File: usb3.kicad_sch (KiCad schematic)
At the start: 50 parts, among them J5 Conn_USB-C_WE_632723300011, Q19 PJE138K, Q4 PJE138K, U17 HD3SS3220RNH, U18 AP22615A_TSOT26, U19 TPD4E05U06QDQARQ1, U20 TPD4E05U06QDQARQ1, U21 TPD4E05U06QDQARQ1

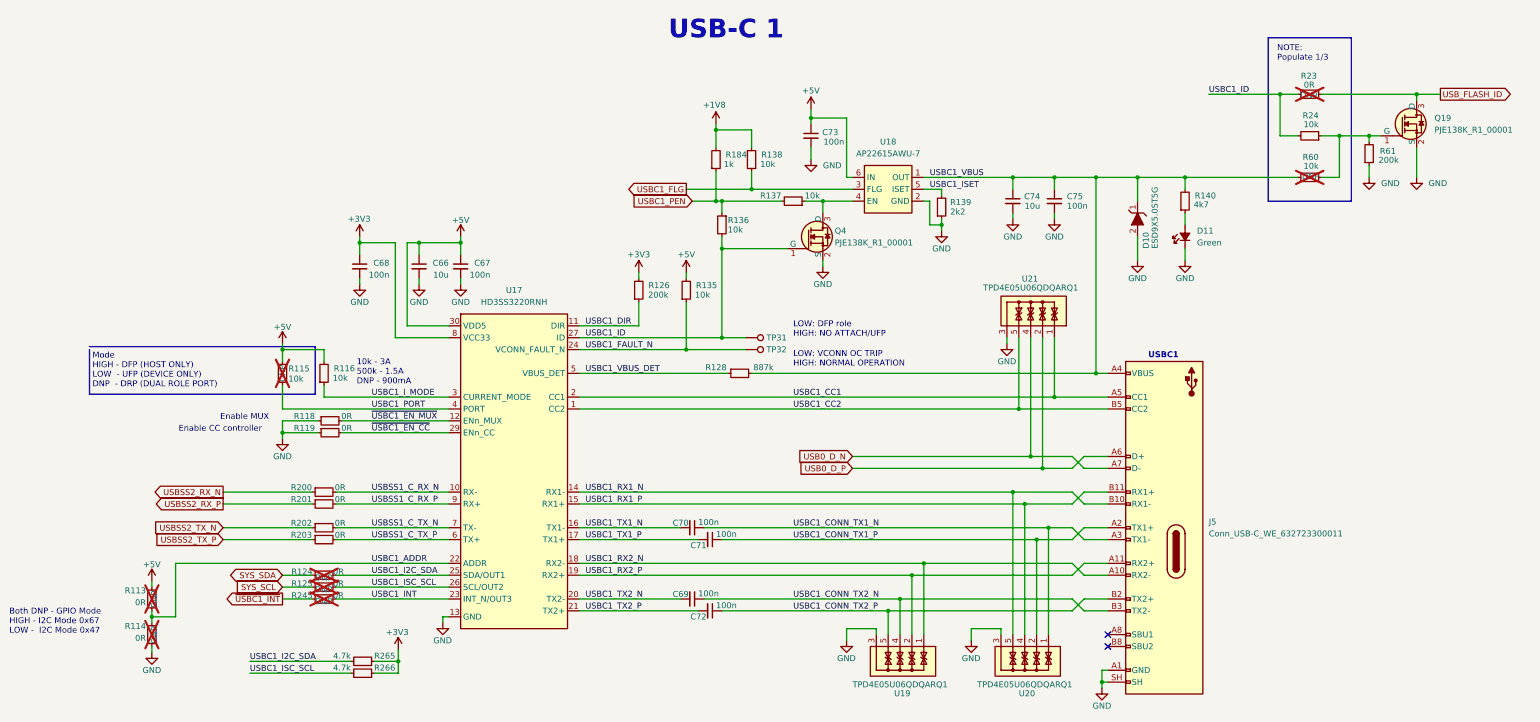
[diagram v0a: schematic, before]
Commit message: Schematic Cleanup, Complete routing
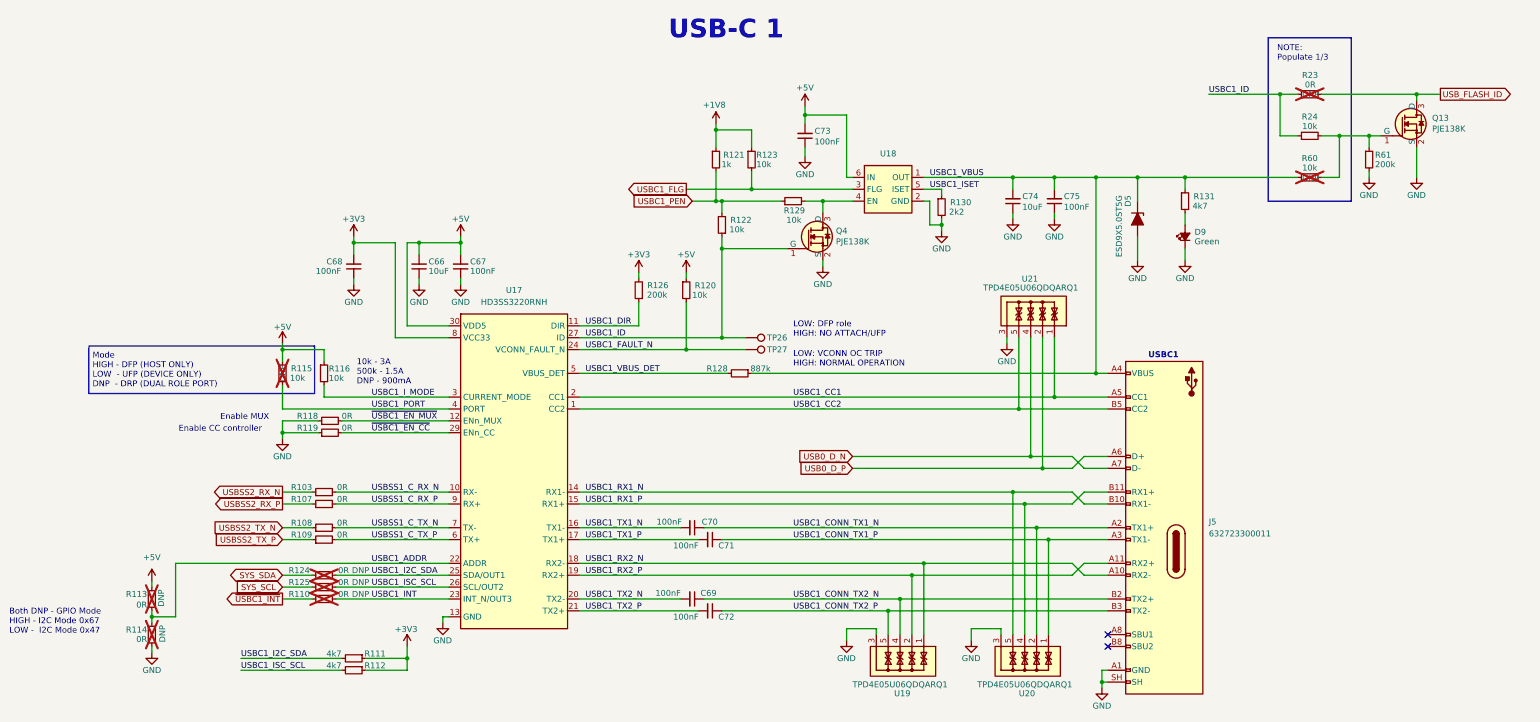
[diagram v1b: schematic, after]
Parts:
- C66, C74: value C_10u_0603 -> 10uF; symbol antmicroCapacitors0603:C_10u_0603 -> Device:C_Small
- C67, C68, C73, C75: value C_100n_0603 -> 100nF; symbol antmicroCapacitors0402:C_100n_0402 -> Device:C_Small
- C69, C70, C71, C72: value C_100n_0402 -> 100nF; symbol antmicroCapacitors0402:C_100n_0402 -> Device:C_Small
- D5: renamed from D10; symbol antmicroTVSDiodes:ESD9X5.0ST5G -> Device:D_Zener_Filled
- D9: renamed from D11; symbol antmicroLEDIndicationDiscrete:LED_G_0603_LTST-C190GKT -> Device:LED_Small_Filled
- J5: value Conn_USB-C_WE_632723300011 -> 632723300011; symbol antmicroUSBConnectors:USB-C_WE_632723300011 -> JetsonCarrier:USB-C_WE_632723300011
- Q13: renamed from Q19; symbol antmicroTransistorsFETsMOSFETsSingle:PJE138K -> JetsonCarrier:PJE138K
- Q4: symbol antmicroTransistorsFETsMOSFETsSingle:PJE138K -> JetsonCarrier:PJE138K
- R103: renamed from R200; value R_0R_0402 -> 0R; symbol antmicroResistors0402:R_0R_0402 -> Device:R_Small
- R107: renamed from R201; value R_0R_0402 -> 0R; symbol antmicroResistors0402:R_0R_0402 -> Device:R_Small
- R108: renamed from R202; value R_0R_0402 -> 0R; symbol antmicroResistors0402:R_0R_0402 -> Device:R_Small
- R109: renamed from R203; value R_0R_0402 -> 0R; symbol antmicroResistors0402:R_0R_0402 -> Device:R_Small
- R110: renamed from R245; value R_0R_0402 -> 0R; symbol antmicroResistors0402:R_0R_0402 -> Device:R_Small; now in the parts list
- R111: renamed from R265; value R_200k_0603 -> 4k7; symbol antmicroResistors0402:R_200k_0402 -> Device:R_Small; Val 4.7k -> 4k7
- R112: renamed from R266; value R_200k_0603 -> 4k7; symbol antmicroResistors0402:R_200k_0402 -> Device:R_Small; Val 4.7k -> 4k7
- R113, R114, R124, R125: value R_0R_0402 -> 0R; symbol antmicroResistors0402:R_0R_0402 -> Device:R_Small; now in the parts list
- R115: value R_10k_0603 -> 10k; footprint Capacitor_SMD:C_0402_1005Metric -> Resistor_SMD:R_0402_1005Metric; symbol antmicroResistors0402:R_10k_0402 -> Device:R_Small; now in the parts list
- R116: value R_10k_0603 -> 10k; footprint Capacitor_SMD:C_0402_1005Metric -> Resistor_SMD:R_0402_1005Metric; symbol antmicroResistors0402:R_10k_0402 -> Device:R_Small
- R118, R119: value R_0R_0402 -> 0R; symbol antmicroResistors0402:R_0R_0402 -> Device:R_Small
- R120: renamed from R135; value R_10k_0603 -> 10k; symbol antmicroResistors0402:R_10k_0402 -> Device:R_Small
- R121: renamed from R184; value R_1k_0603 -> 1k; symbol antmicroResistors0402:R_1k_0402 -> Device:R_Small
- R122: renamed from R136; value R_10k_0603 -> 10k; symbol antmicroResistors0402:R_10k_0402 -> Device:R_Small
- R123: renamed from R138; value R_10k_0603 -> 10k; footprint Capacitor_SMD:C_0402_1005Metric -> Resistor_SMD:R_0402_1005Metric; symbol antmicroResistors0402:R_10k_0402 -> Device:R_Small
- R126: value R_200k_0603 -> 200k; footprint Capacitor_SMD:C_0402_1005Metric -> Resistor_SMD:R_0402_1005Metric; symbol antmicroResistors0402:R_200k_0402 -> Device:R_Small
- R128: value R_887k_0603 -> 887k; symbol antmicroResistors0402:R_887k_0402 -> Device:R_Small
- R129: renamed from R137; value R_10k_0603 -> 10k; symbol antmicroResistors0402:R_10k_0402 -> Device:R_Small
- R130: renamed from R139; value R_2k2_0603 -> 2k2; symbol antmicroResistors0402:R_2k2_0402 -> Device:R_Small
- R131: renamed from R140; value R_4k7_0603 -> 4k7; footprint Capacitor_SMD:C_0402_1005Metric -> Resistor_SMD:R_0402_1005Metric; symbol antmicroResistors0402:R_470R_0402 -> Device:R_Small
- R23: value R_0R_0603 -> 0R; symbol antmicroResistors0402:R_0R_0402 -> Device:R_Small; now in the parts list
- R24: value R_10k_0603 -> 10k; symbol antmicroResistors0402:R_10k_0402 -> Device:R_Small
- R60: value R_10k_0603 -> 10k; symbol antmicroResistors0402:R_10k_0402 -> Device:R_Small; now in the parts list
- R61: value R_200k_0603 -> 200k; symbol antmicroResistors0402:R_200k_0402 -> Device:R_Small
- TP26: renamed from TP31; symbol antmicroTestPoints:TP_0.75mm_SMD -> Connector:TestPoint
- TP27: renamed from TP32; symbol antmicroTestPoints:TP_0.75mm_SMD -> Connector:TestPoint
- U17: symbol antmicroInterfaceControllers:HD3SS3220RNH -> JetsonCarrier:HD3SS3220RNH
- U18: symbol antmicroPMICPowerDistributionSwitchesLoadDrivers:AP22615A_TSOT26 -> JetsonCarrier:AP22615A_TSOT26
- U19, U20, U21: symbol antmicroTVSDiodes:TPD4E05U06QDQARQ1 -> JetsonCarrier:TPD4E05U06QDQARQ1
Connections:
- net +1V8: now also R121.1, R123.1; no longer R121.2, R123.2
- net +3V3: now also C68.2; no longer C68.1
- net +5V: now also C66.2, C67.2, C73.2, R115.2, R116.1, R120.1; no longer C66.1, C67.1, C73.1, R115.1, R116.2, R120.2
- net GND: now also C66.1, C67.1, C68.1, C73.1, C74.1, C75.1, R130.2, R61.2; no longer C66.2, C67.2, C68.2, C73.2, C74.2, C75.2, R130.1, R61.1
- net USBC1_CONN_TX1_N: now also J5.A2 (TX1+), U20.2, U20.9; no longer J5.A3 (TX1-), U20.1, U20.10
- net USBC1_CONN_TX1_P: now also J5.A3 (TX1-), U20.1, U20.10; no longer J5.A2 (TX1+), U20.2, U20.9
- net USBC1_CONN_TX2_N: now also J5.B2 (TX2+); no longer J5.B3 (TX2-)
- net USBC1_CONN_TX2_P: now also J5.B3 (TX2-); no longer J5.B2 (TX2+)
- net USBC1_FAULT_N: now also R120.2; no longer R120.1
- net USBC1_FLG: now also R123.2; no longer R123.1
- net USBC1_ID: now also R122.1, R24.1; no longer R122.2, R24.2
- net USBC1_ISET: now also R130.1; no longer R130.2
- net USBC1_I_MODE: now also R116.2; no longer R116.1
- net USBC1_PEN: now also R121.2, R122.2, R129.1; no longer R121.1, R122.1, R129.2
- net USBC1_PORT: now also R115.1; no longer R115.2
- net USBC1_VBUS: now also C74.2, C75.2, R128.1, R131.1, R60.1; no longer C74.1, C75.1, R128.2, R131.2, R60.2
- net USBC1_VBUS_DET: now also R128.2; no longer R128.1
- net at D9.2 (A): now also R131.2; no longer R131.1
- net at Q4.3 (D), U18.4 (EN): now also R129.2; no longer R129.1
- new net: Q13.1 (G), R24.2, R60.2, R61.1
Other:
- moved on the sheet: C66, C67, C68, C69, C70, C71, C72, C73, C74, C75, R103, R107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
